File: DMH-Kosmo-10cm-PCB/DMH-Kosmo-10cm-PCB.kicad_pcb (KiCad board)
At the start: 2 copper layers, 96 x 175 mm, 0 parts

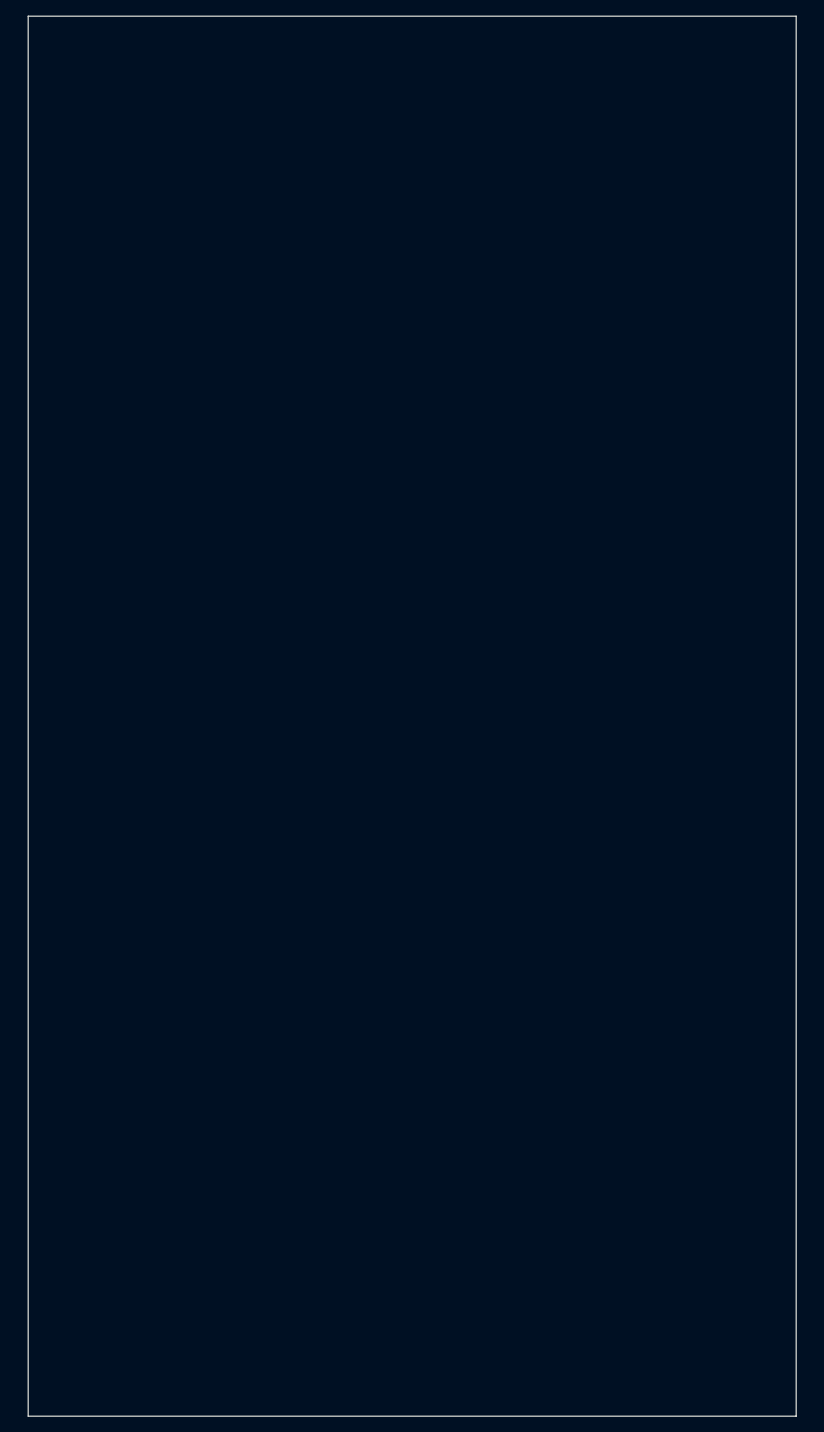
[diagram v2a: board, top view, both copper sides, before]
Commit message: Enlarged PCB limits
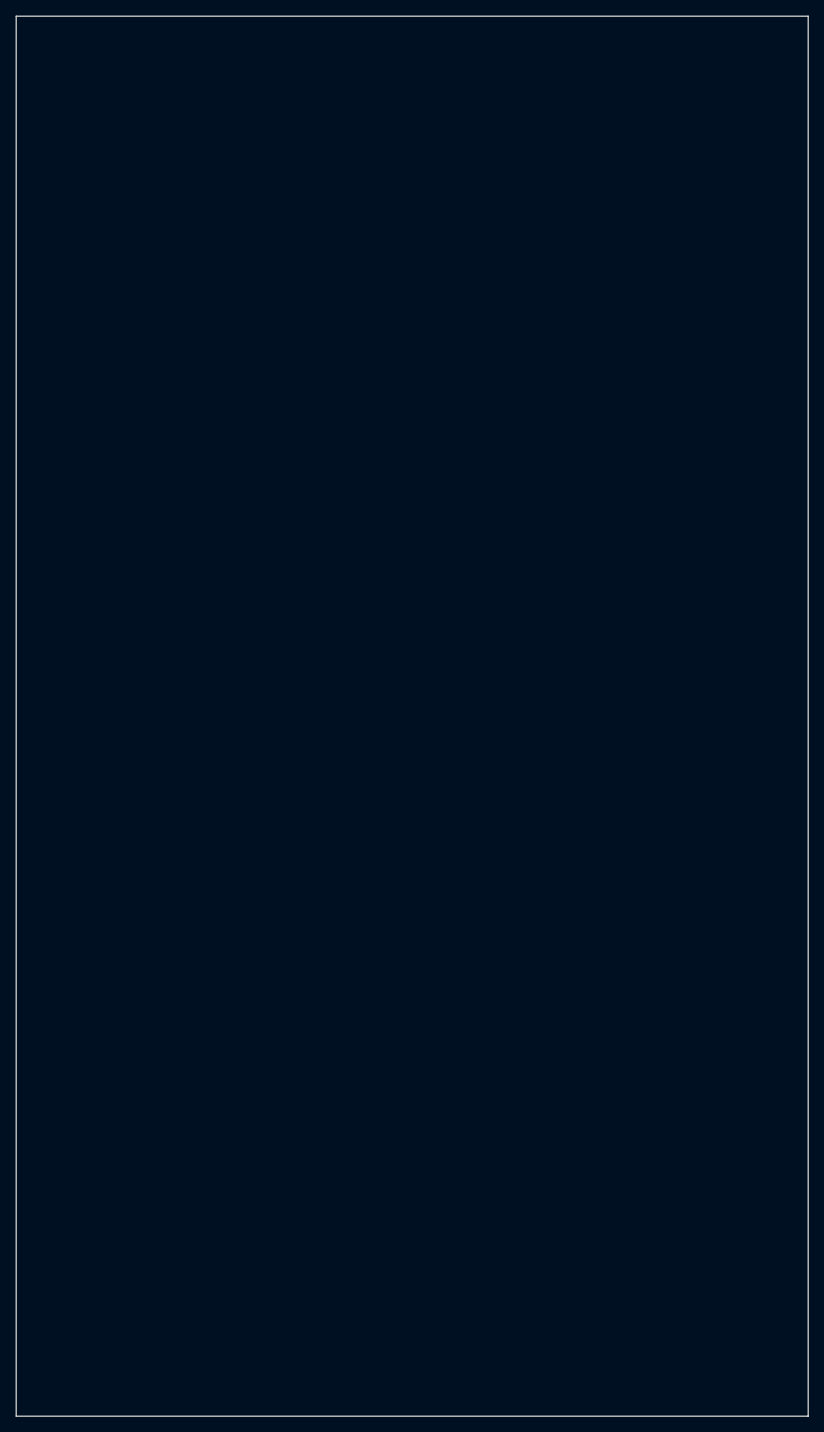
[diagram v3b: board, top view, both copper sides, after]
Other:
- board size 96 x 175 mm -> 99 x 175 mm
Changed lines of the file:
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@@
 	)
 	(gr_rect
-		(start 52 42.5)
-		(end 148 217.5)
+		(start 50.5 42.5)
+		(end 149.5 217.5)
 		(stroke
 			(width 0.05)

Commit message: Added 15cm templates
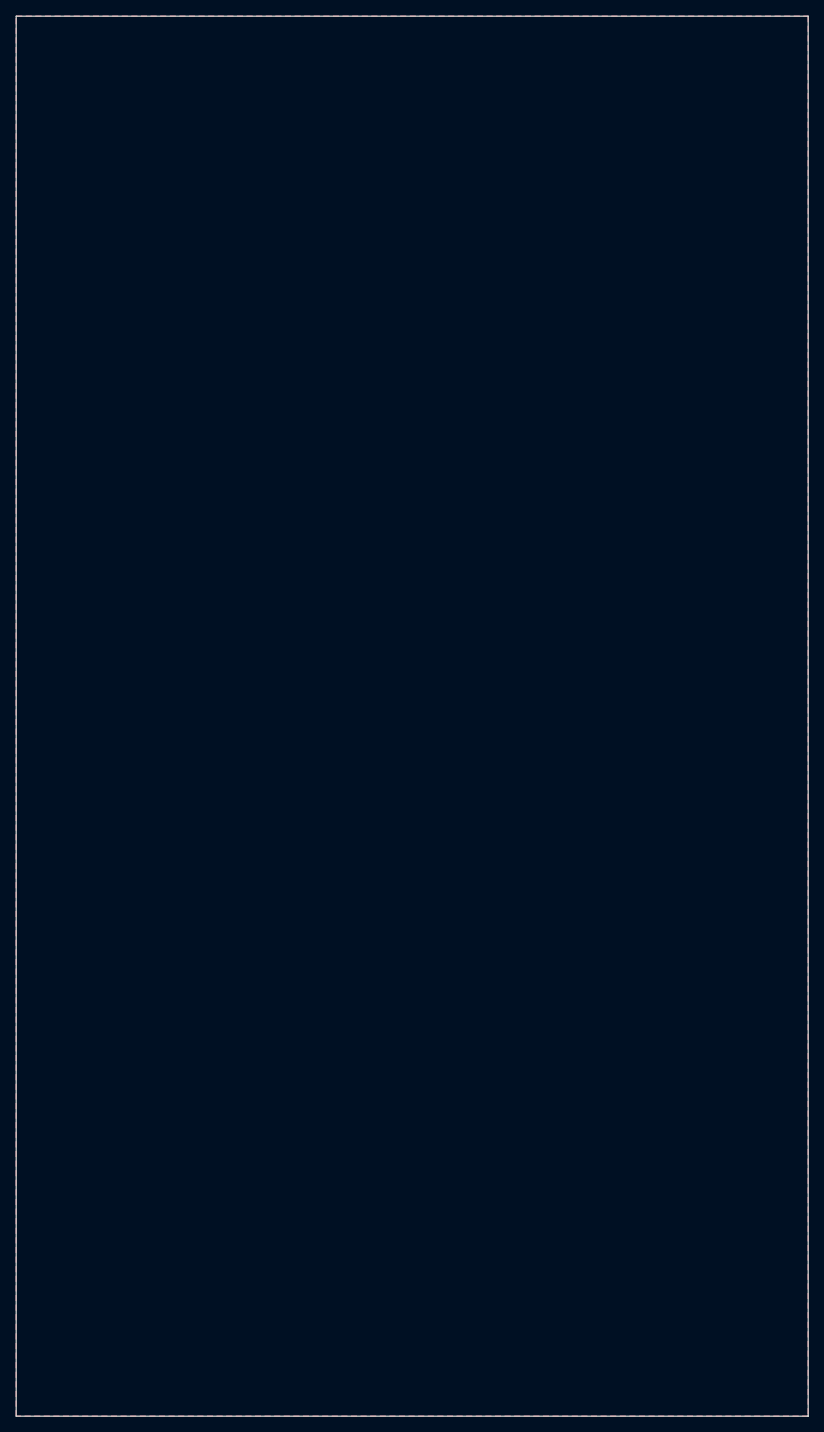
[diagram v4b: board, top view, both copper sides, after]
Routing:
- added copper zone on B.Cu, net GND
- added copper zone on F.Cu, net GND
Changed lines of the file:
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@@
 		(layer "B.SilkS")
+	)
+	(gr_circle
+		(center 58.5 171.75)
+		(end 63.25 171.75)
+		(stroke
+			(width 0.1)
+			(type default)
+		)
+		(fill no)
+		(layer "Cmts.User")
+	)
+	(gr_circle
+		(center 58.5 190.25)
+		(end 63.25 190.25)
+		(stroke
+			(width 0.1)
+			(type default)
+		)
+		(fill no)
+		(layer "Cmts.User")
+	)
+	(gr_circle
+		(center 58.5 208.75)
+		(end 63.25 208.75)
+		(stroke
+			(width 0.1)
+			(type default)
+		)
+		(fill no)
+		(layer "Cmts.User")
+	)
+	(gr_circle
+		(center 75 171.75)
+		(end 79.75 171.75)
+		(stroke
+			(width 0.1)
+			(type default)
+		)
+		(fill no)
+		(layer "Cmts.User")
+	)
+	(gr_circle
+		(center 75 190.25)
+		(end 79.75 190.25)
+		(stroke
+			(width 0.1)
+			(type default)
+		)
+		(fill no)
+		(layer "Cmts.User")
+	)
+	(gr_circle
+		(center 75 208.75)
+		(end 79.75 208.75)
+		(stroke
+			(width 0.1)
+			(type default)
+		)
+		(fill no)
+		(layer "Cmts.User")
+	)
+	(gr_circle
+		(center 91.5 171.75)
+		(end 96.25 171.75)
+		(stroke
+			(width 0.1)
+			(type default)
+		)
+		(fill no)
+		(layer "Cmts.User")
+	)
+	(gr_circle
+		(center 91.5 190.25)
+		(end 96.25 190.25)
+		(stroke
+			(width 0.1)
+			(type default)
+		)
+		(fill no)
+		(layer "Cmts.User")
+	)
+	(gr_circle
+		(center 91.5 208.75)
+		(end 96.25 208.75)
+		(stroke
+			(width 0.1)
+			(type default)
+		)
+		(fill no)
+		(layer "Cmts.User")
+	)
+	(gr_circle
+		(center 108.5 171.75)
+		(end 113.25 171.75)
+		(stroke
+			(width 0.1)
+			(type default)
+		)
+		(fill no)
+		(layer "Cmts.User")
+	)
+	(gr_circle
+		(center 108.5 190.25)
+		(end 113.25 190.25)
+		(stroke
+			(width 0.1)
+			(type default)
+		)
+		(fill no)
+		(layer "Cmts.User")
+	)
+	(gr_circle
+		(center 108.5 208.75)
+		(end 113.25 208.75)
+		(stroke
+			(width 0.1)
+			(type default)
+		)
+		(fill no)
+		(layer "Cmts.User")
+	)
+	(gr_circle
+		(center 125 171.75)
+		(end 129.75 171.75)
+		(stroke
+			(width 0.1)
+			(type default)
+		)
+		(fill no)
+		(layer "Cmts.User")
+	)
+	(gr_circle
+		(center 125 190.25)
+		(end 129.75 190.25)
+		(stroke
+			(width 0.1)
+			(type default)
+		)
+		(fill no)
+		(layer "Cmts.User")
+	)
+	(gr_circle
+		(center 125 208.75)
+		(end 129.75 208.75)
+		(stroke
+			(width 0.1)
+			(type default)
+		)
+		(fill no)
+		(layer "Cmts.User")
+	)
+	(gr_circle
+		(center 141.5 171.75)
+		(end 146.25 171.75)
+		(stroke
+			(width 0.1)
+			(type default)
+		)
+		(fill no)
+		(layer "Cmts.User")
+	)
+	(gr_circle
+		(center 141.5 190.25)
+		(end 146.25 190.25)
+		(stroke
+			(width 0.1)
+			(type default)
+		)
+		(fill no)
+		(layer "Cmts.User")
+	)
+	(gr_circle
+		(center 141.5 208.75)
+		(end 146.25 208.75)
+		(stroke
+			(width 0.1)
+			(type default)
+		)
+		(fill no)
+		(layer "Cmts.User")
 	)
 	(gr_rect
@@
 		)
 	)
+	(zone
+		(net "GND")
+		(layers "F.Cu" "B.Cu")
+		(name "Ground_planes")
+		(hatch edge 0.5)
+		(connect_pads
+			(clearance 0.5)
+		)
+		(min_thickness 0.25)
+		(fill yes
+			(thermal_gap 0.5)
+			(thermal_bridge_width 0.5)
+			(island_removal_mode 0)
+		)
+		(polygon
+			(pts
+				(xy 50.5 42.5) (xy 149.5 42.5) (xy 149.5 217.5) (xy 50.5 217.5)
+			)
+		)
+	)
